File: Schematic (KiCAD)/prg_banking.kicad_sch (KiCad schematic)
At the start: 68 parts

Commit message: - Started work on the pulse channels.  - Solved at least 2 of the red traces in the SVG.  - Finally realized that "Unknown 4to1" cells are actually just ordinary And-Or-Invert "AOI22" cells.
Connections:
- net at A48. (X): now also A54. (X); no longer A49. (X)
- net at B90. (X): now also A51. (X); no longer B92. (X)
- net at A52. (X): now also A53. (X); no longer A50. (X)
- net at D21. (X): now also A27. (Y1); no longer D20. (X)
- net at D25. (X): now also D26. (X); no longer D24. (X)
- net at D26. (X): now also A24. (Y1); no longer D25. (X)
- new net: B38. (Y2), D34. (X)
- new net: A25. (Y1), D22. (X)
- new net: A34. (Y4), A35. (Y4), A36. (Y4), D37. (X)
- new net: A22. (Y4), A23. (Y2), A37. (Y4), D30. (X)
- new net: D32. (X), D33. (X)
- new net: D16. (X), D32. (X)
- new net: A48. (X), A49. (X)
- new net: A48. (X), A51. (X)
- new net: B90. (X), B92. (X)
- new net: D4. (Q1), D9. (X)
- new net: A50. (X), A52. (X)
- new net: A29. (Y4), A30. (Y4), A31. (Y4), D31. (X)
- new net: D17. (X), D18. (X)
- new net: D20. (X), D21. (X)
- new net: D19. (X), D20. (X)
- new net: A41. (X), A42. (X), A43. (X)
- new net: D27. (X), D29. (X)
- new net: D11. (X), D4. (Q1)
- new net: D28. (X), D29. (X)
- new net: A45. (X), A49. (X), A53. (X)
- new net: A32. (Y5), A33. (Y5), D36. (X)
- new net: D24. (X), D25. (X)
- new net: D23. (X), D25. (X)
- new net: D15. (X), D23. (X)
- new net: A43. (X), A44. (X), A47. (X)

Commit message: - Pulse DAC logic is now complete.  - The 4-bit adders are verified correct using Excel.    - This revealed 1 tracing error and also 3 XNOR gates that are actually XOR in this case.  - Now including a PDF version of the schematic.
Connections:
- net at A48. (X): now also A54. (X); no longer A49. (X)
- net at B90. (X): now also A51. (X); no longer B92. (X)
- net at A52. (X): now also A53. (X); no longer A50. (X)
- net at D21. (X): now also A27. (Y1); no longer D20. (X)
- net at D25. (X): now also D26. (X); no longer D24. (X)
- net at D26. (X): now also A24. (Y1); no longer D25. (X)
- new net: B38. (Y2), D34. (X)
- new net: A25. (Y1), D22. (X)
- new net: A34. (Y4), A35. (Y4), A36. (Y4), D37. (X)
- new net: A22. (Y4), A23. (Y2), A37. (Y4), D30. (X)
- new net: D32. (X), D33. (X)
- new net: D16. (X), D32. (X)
- new net: A48. (X), A49. (X)
- new net: A48. (X), A51. (X)
- new net: B90. (X), B92. (X)
- new net: D4. (Q1), D9. (X)
- new net: A50. (X), A52. (X)
- new net: A29. (Y4), A30. (Y4), A31. (Y4), D31. (X)
- new net: D17. (X), D18. (X)
- new net: D20. (X), D21. (X)
- new net: D19. (X), D20. (X)
- new net: A41. (X), A42. (X), A43. (X)
- new net: D27. (X), D29. (X)
- new net: D11. (X), D4. (Q1)
- new net: D28. (X), D29. (X)
- new net: A45. (X), A49. (X), A53. (X)
- new net: A32. (Y5), A33. (Y5), D36. (X)
- new net: D24. (X), D25. (X)
- new net: D23. (X), D25. (X)
- new net: D15. (X), D23. (X)
- new net: A43. (X), A44. (X), A47. (X)

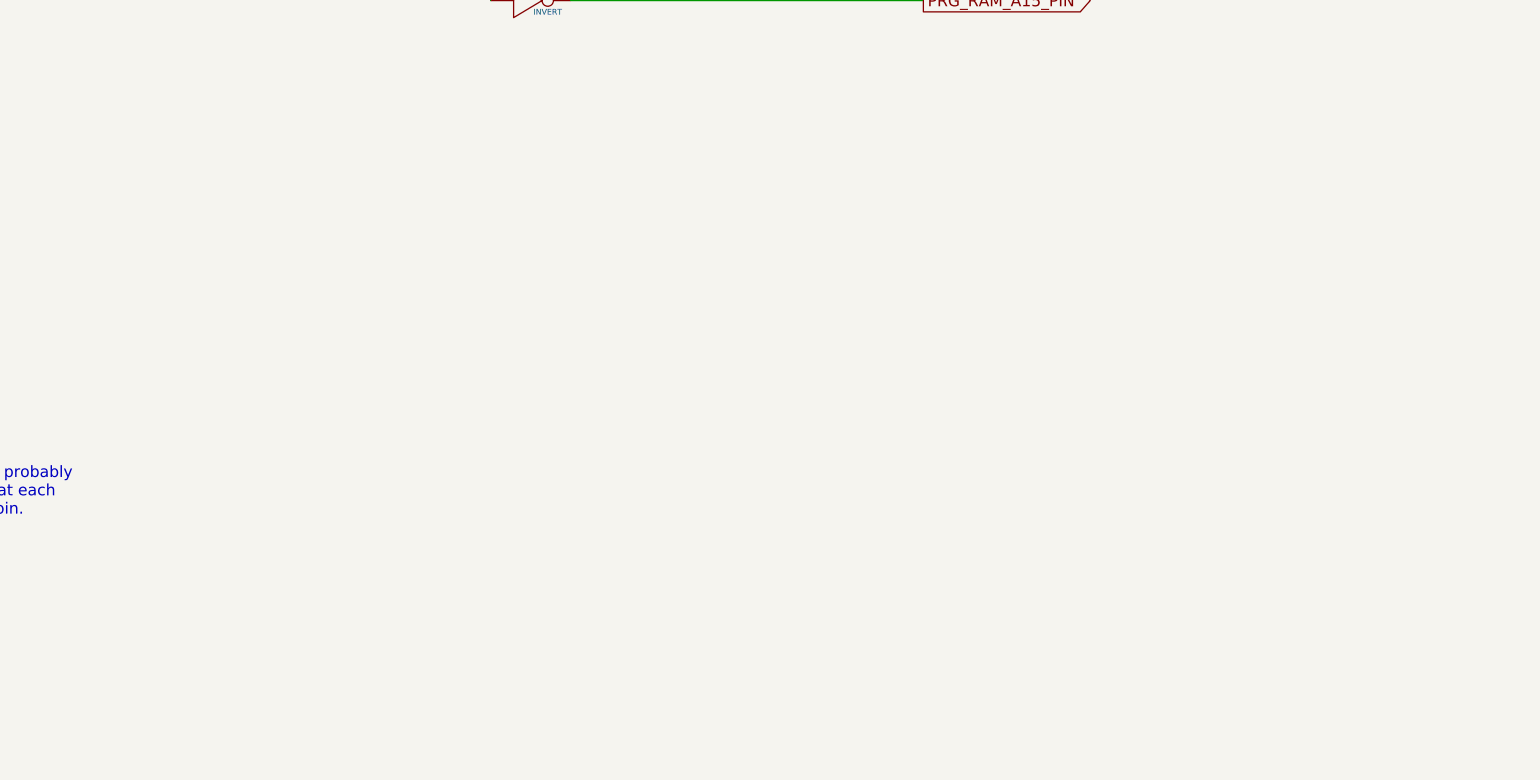
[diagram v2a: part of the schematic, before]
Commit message: - All cells in the left and center areas have now been added into the schematics.  - Changed naming of the PDF files; I was accidentally writing over furrtek's original with my new PDF.
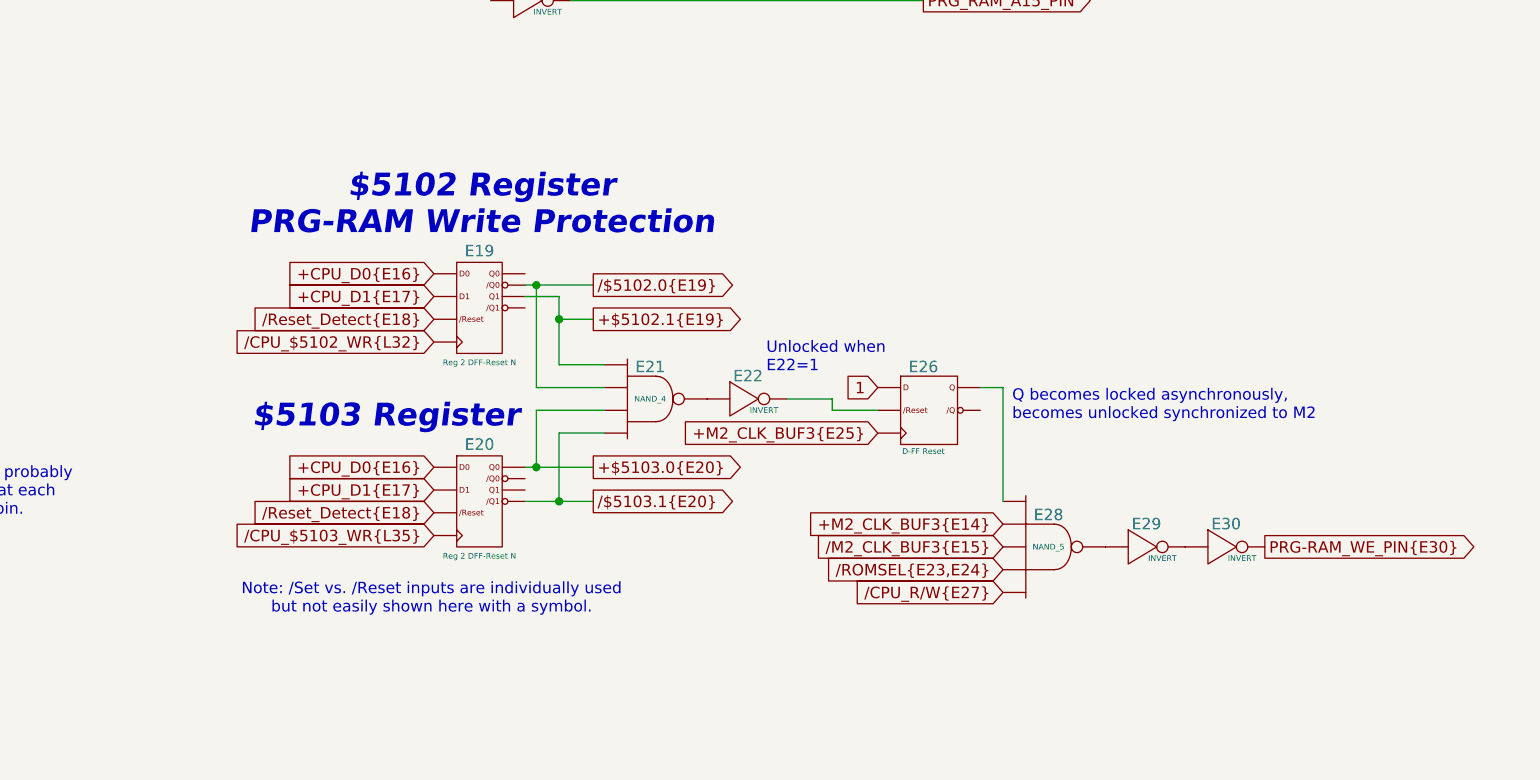
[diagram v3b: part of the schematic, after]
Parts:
- added E19, E20: Reg 2 DFF-Reset N, symbol MMC5:Reg_2_DFF-Reset_N
- added E21: NAND_4, symbol MMC5:NAND_4
- added E22, E29, E30: INVERT, symbol MMC5:INVERT
- added E26: D-FF Reset, symbol MMC5:D-FF_Reset
- added E28: NAND_5, symbol MMC5:NAND_5
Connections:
- net at A48. (X): now also A54. (X); no longer A49. (X)
- net at B90. (X): now also A51. (X); no longer B92. (X)
- net at A52. (X): now also A53. (X); no longer A50. (X)
- net at D21. (X): now also A27. (Y1); no longer D20. (X)
- net at D25. (X): now also D26. (X); no longer D24. (X)
- net at D26. (X): now also A24. (Y1); no longer D25. (X)
- new net: B38. (Y2), D34. (X)
- new net: A25. (Y1), D22. (X)
- new net: A34. (Y4), A35. (Y4), A36. (Y4), D37. (X)
- new net: E26. (/Q), E28. (X)
- new net: E28. (X), E29. (X)
- new net: A22. (Y4), A23. (Y2), A37. (Y4), D30. (X)
- new net: E22. (X), E26. (/Q)
- new net: E21. (X), E22. (X)
- new net: D32. (X), D33. (X)
- new net: D16. (X), D32. (X)
- new net: A48. (X), A49. (X)
- new net: A48. (X), A51. (X)
- new net: B90. (X), B92. (X)
- new net: D4. (Q1), D9. (X)
- new net: A50. (X), A52. (X)
- new net: A29. (Y4), A30. (Y4), A31. (Y4), D31. (X)
- new net: D17. (X), D18. (X)
- new net: D20. (X), D21. (X)
- new net: D19. (X), D20. (X)
- new net: A41. (X), A42. (X), A43. (X)
- new net: D27. (X), D29. (X)
- new net: D11. (X), D4. (Q1)
- new net: D28. (X), D29. (X)
- new net: A45. (X), A49. (X), A53. (X)
- new net: A32. (Y5), A33. (Y5), D36. (X)
- new net: D24. (X), D25. (X)
- new net: D23. (X), D25. (X)
- new net: E29. (X), E30. (X)
- new net: D15. (X), D23. (X)
- new net: A43. (X), A44. (X), A47. (X)
- new net +$5102.1{E19}: E19. (/Q1), E21. (X)
- new net +$5103.0{E20}: E20. (/Q1), E21. (X)
- new net +CPU_D0{E16}: E19. (/Q1), E20. (/Q1)
- new net +CPU_D1{E17}: E19. (/Q1), E20. (/Q1)
- new net +M2_CLK_BUF3{E14}: E28. (X)
- new net +M2_CLK_BUF3{E25}: E26. (/Q)
- new net 1: E26. (/Q)
- new net PRG-RAM_WE_PIN{E30}: E30. (X)
- new net /$5102.0{E19}: E19. (/Q1), E21. (X)
- new net /$5103.1{E20}: E20. (/Q1), E21. (X)
- new net /CPU_$5102_WR{L32}: E19. (/Q1)
- new net /CPU_$5103_WR{L35}: E20. (/Q1)
- new net /CPU_R/W{E27}: E28. (X)
- new net /M2_CLK_BUF3{E15}: E28. (X)
- new net /ROMSEL{E23,E24}: E28. (X)
- new net /Reset_Detect{E18}: E19. (/Q1), E20. (/Q1)
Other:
- note added: "$5102 Register PRG-RAM Write Protection"
- note added: "$5103 Register"
- note added: "Note: /Set vs. /Reset inputs are individually used but not easily shown here with a symbol."
- note added: "Q becomes locked asynchronously, becomes unlocked synchronized to M2"
- note added: "Unlocked when E22=1"
